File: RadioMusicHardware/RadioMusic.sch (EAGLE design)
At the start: 59 parts, among them IC1 TL074P, IC2 7805L

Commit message: Untested fade circuit + more PCB layout
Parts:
- removed BANK_BUTTON: D6_PUSH_SWITCH, TomW:D6_PUSH_SWITCH
- removed IC1: TL074P, linear:TL074P
- removed R15: 10k, TomW:R-EU_STANDARD_RESISTOR
- added IC3, IC4: TL072P, TomW:TL072P
- added JP1, JP2, JP3, JP4: (no value), SparkFun-Connectors:M08LOCK
- R6: value 8.2k -> 330K
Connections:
- net +3.3V: no longer BANK_BUTTON.P
- net GND: no longer R15.1
- net N$12: now also IC3B.+IN; no longer IC1B.+IN
- net N$2: now also IC4A.+IN; no longer IC1C.+IN
- net N$3: now also IC3A.+IN; no longer IC1A.+IN
- net N$5: now also IC4A.-IN, IC4A.OUT; no longer IC1C.-IN, IC1C.OUT
- net N$6: now also IC4B.+IN; no longer IC1D.+IN
- net N$7: now also IC4B.-IN; no longer IC1D.-IN
- net N$8: now also IC4B.OUT; no longer IC1D.OUT
- net PIN2: no longer BANK_BUTTON.O, R15.2
- net PIN22/A8: now also IC3A.-IN, IC3A.OUT, IC3B.-IN, IC3B.OUT; no longer IC1A.-IN, IC1A.OUT, IC1B.-IN, IC1B.OUT
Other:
- note added: "Front Board requirements: +3.3v for pots & SD Card GND LED1 LED2 LED3 LED4 LEDReset Reset Button Reset CV Time CV Time Pot ChannelCV Channel Pot SD - MISO SD- MOSI SD-CLOCK SD-SS"
- note removed: "NB Outline is for Teensy3 Teensy3.1 has DAC output where Reset was on Teensy3"
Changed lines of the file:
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@@
 <part name="RESET" library="thonkiconn" deviceset="WQP-PJ301M-12_JACK" device=""/>
 <part name="OUT1" library="thonkiconn" deviceset="WQP-PJ301M-12_JACK" device=""/>
-<part name="IC1" library="linear" deviceset="TL074" device="P"/>
 <part name="IC2" library="gm-regulators" deviceset="78*" device="L" technology="05"/>
 <part name="R1" library="TomW" deviceset="R-EU_" device="STANDARD_RESISTOR" value="100k"/>
@@
 <part name="SUPPLY6" library="supply2" deviceset="GND" device=""/>
 <part name="C7" library="TomW" deviceset="C-EU" device="050-025X075" value="100n"/>
-<part name="R6" library="TomW" deviceset="R-EU_" device="STANDARD_RESISTOR" value="8.2k"/>
+<part name="R6" library="TomW" deviceset="R-EU_" device="STANDARD_RESISTOR" value="330K"/>
 <part name="SUPPLY7" library="supply2" deviceset="GND" device=""/>
 <part name="R7" library="TomW" deviceset="R-EU_" device="STANDARD_RESISTOR" value="1k"/>
@@
 <part name="SUPPLY15" library="supply2" deviceset="GND" device=""/>
 <part name="R14" library="TomW" deviceset="R-EU_" device="STANDARD_RESISTOR" value="220R"/>
-<part name="BANK_BUTTON" library="TomW" deviceset="D6_PUSH_SWITCH" device="" value="D6_PUSH_SWITCH"/>
-<part name="R15" library="TomW" deviceset="R-EU_" device="STANDARD_RESISTOR" value="10k"/>
-<part name="SUPPLY18" library="supply2" deviceset="GND" device=""/>
 <part name="RESET_BUTTON" library="TomW" deviceset="D6_PUSH_SWITCH" device="" value="D6_PUSH_SWITCH"/>
 <part name="R16" library="TomW" deviceset="R-EU_" device="STANDARD_RESISTOR" value="10k"/>
@@
 <part name="RESET_LED" library="TomW" deviceset="LED" device="3MM"/>
 <part name="R21" library="TomW" deviceset="R-EU_" device="STANDARD_RESISTOR" value="1k"/>
+<part name="JP1" library="SparkFun-Connectors" deviceset="M08" device="LOCK"/>
+<part name="JP2" library="SparkFun-Connectors" deviceset="M08" device="LOCK"/>
+<part name="JP3" library="SparkFun-Connectors" deviceset="M08" device="LOCK"/>
+<part name="JP4" library="SparkFun-Connectors" deviceset="M08" device="LOCK"/>
+<part name="IC3" library="TomW" deviceset="TL072" device="P"/>
+<part name="IC4" library="TomW" deviceset="TL072" device="P"/>
 </parts>
 <sheets>
@@
 Don't get it the wrong way around!
 Ferrites: 81-BL01RN1A1D2B  or 623-2743001112LF</text>
-<text x="203.2" y="185.42" size="0.762" layer="91">NB Outline is for Teensy3
-Teensy3.1 has DAC output
-where Reset was on Teensy3</text>
 <text x="243.84" y="137.16" size="1.27" layer="91"> SD Card Connections:
  SCLK 14
@@
  MOSI 7
  SS   10 </text>
+<text x="248.92" y="182.88" size="0.762" layer="91">Front Board requirements:
++3.3v for pots &amp; SD Card
+GND
+LED1
+LED2
+LED3
+LED4
+LEDReset
+Reset Button
+Reset CV
+Time CV
+Time Pot
+ChannelCV
+Channel Pot
+SD - MISO
+SD- MOSI
+SD-CLOCK
+SD-SS
+</text>
 </plain>
 <instances>
@@
 <instance part="RESET" gate="G$1" x="119.38" y="134.62" rot="MR0"/>
 <instance part="OUT1" gate="G$1" x="269.24" y="66.04"/>
-<instance part="IC1" gate="A" x="66.04" y="157.48"/>
-<instance part="IC1" gate="C" x="182.88" y="71.12"/>
-<instance part="IC1" gate="D" x="231.14" y="68.58"/>
+<instance part="IC3" gate="A" x="66.04" y="157.48"/>
+<instance part="IC4" gate="A" x="182.88" y="71.12"/>
+<instance part="IC4" gate="B" x="231.14" y="68.58"/>
 <instance part="IC2" gate="A1" x="91.44" y="38.1"/>
 <instance part="R1" gate="G$1" x="45.72" y="160.02"/>
@@
 <instance part="TIME" gate="G$1" x="20.32" y="66.04"/>
 <instance part="TIME_CV" gate="G$1" x="20.32" y="96.52" rot="MR0"/>
-<instance part="IC1" gate="B" x="66.04" y="96.52"/>
+<instance part="IC3" gate="B" x="66.04" y="96.52"/>
 <instance part="R10" gate="G$1" x="45.72" y="99.06"/>
 <instance part="SUPPLY9" gate="GND" x="25.4" y="88.9"/>
@@
 <instance part="SUPPLY15" gate="GND" x="157.48" y="116.84"/>
 <instance part="R14" gate="G$1" x="134.62" y="137.16"/>
-<instance part="BANK_BUTTON" gate="G$1" x="127" y="198.12"/>
-<instance part="R15" gate="G$1" x="134.62" y="190.5" rot="R90"/>
-<instance part="SUPPLY18" gate="GND" x="134.62" y="180.34"/>
 <instance part="RESET_BUTTON" gate="G$1" x="165.1" y="198.12"/>
 <instance part="R16" gate="G$1" x="172.72" y="190.5" rot="R90"/>
@@
 <instance part="RESET_LED" gate="G$1" x="185.42" y="144.78" rot="R270"/>
 <instance part="R21" gate="G$1" x="170.18" y="144.78"/>
+<instance part="JP1" gate="G$1" x="304.8" y="190.5"/>
+<instance part="JP2" gate="G$1" x="317.5" y="198.12"/>
+<instance part="JP3" gate="G$1" x="307.34" y="167.64"/>
+<instance part="JP4" gate="G$1" x="320.04" y="170.18"/>
 </instances>
 <busses>
@@
 <wire x1="157.48" y1="121.92" x2="157.48" y2="119.38" width="0.1524" layer="91"/>
 <pinref part="SUPPLY15" gate="GND" pin="GND"/>
-</segment>
-<segment>
-<pinref part="R15" gate="G$1" pin="1"/>
-<wire x1="134.62" y1="185.42" x2="134.62" y2="182.88" width="0.1524" layer="91"/>
-<pinref part="SUPPLY18" gate="GND" pin="GND"/>
 </segment>
 <segment>
@@
 </segment>
 <segment>
-<pinref part="BANK_BUTTON" gate="G$1" pin="P"/>
-<wire x1="119.38" y1="198.12" x2="121.92" y2="198.12" width="0.1524" layer="91"/>
-<label x="119.38" y="198.12" size="1.27" layer="95" rot="R180" xref="yes"/>
-</segment>
-<segment>
 <pinref part="RESET_BUTTON" gate="G$1" pin="P"/>
 <wire x1="157.48" y1="198.12" x2="160.02" y2="198.12" width="0.1524" layer="91"/>
@@
 <segment>
 <pinref part="R1" gate="G$1" pin="2"/>
-<pinref part="IC1" gate="A" pin="+IN"/>
+<pinref part="IC3" gate="A" pin="+IN"/>
 <wire x1="58.42" y1="160.02" x2="50.8" y2="160.02" width="0.1524" layer="91"/>
 </segment>
@@
 <net name="PIN22/A8" class="0">
 <segment>
-<pinref part="IC1" gate="A" pin="-IN"/>
+<pinref part="IC3" gate="A" pin="-IN"/>
 <wire x1="58.42" y1="154.94" x2="53.34" y2="154.94" width="0.1524" layer="91"/>
 <wire x1="53.34" y1="154.94" x2="53.34" y2="147.32" width="0.1524" layer="91"/>
 <wire x1="53.34" y1="147.32" x2="78.74" y2="147.32" width="0.1524" layer="91"/>
 <wire x1="78.74" y1="147.32" x2="78.74" y2="157.48" width="0.1524" layer="91"/>
-<pinref part="IC1" gate="A" pin="OUT"/>
+<pinref part="IC3" gate="A" pin="OUT"/>
 <wire x1="78.74" y1="157.48" x2="73.66" y2="157.48" width="0.1524" layer="91"/>
 <pinref part="R9" gate="G$1" pin="1"/>
@@
 </segment>
 <segment>
-<pinref part="IC1" gate="B" pin="-IN"/>
+<pinref part="IC3" gate="B" pin="-IN"/>
 <wire x1="58.42" y1="93.98" x2="53.34" y2="93.98" width="0.1524" layer="91"/>
 <wire x1="53.34" y1="93.98" x2="53.34" y2="86.36" width="0.1524" layer="91"/>
 <wire x1="53.34" y1="86.36" x2="78.74" y2="86.36" width="0.1524" layer="91"/>
 <wire x1="78.74" y1="86.36" x2="78.74" y2="96.52" width="0.1524" layer="91"/>
-<pinref part="IC1" gate="B" pin="OUT"/>
+<pinref part="IC3" gate="B" pin="OUT"/>
 <wire x1="78.74" y1="96.52" x2="73.66" y2="96.52" width="0.1524" layer="91"/>
 <pinref part="R12" gate="G$1" pin="1"/>
@@
 <net name="N$2" class="0">
 <segment>
-<pinref part="IC1" gate="C" pin="+IN"/>
+<pinref part="IC4" gate="A" pin="+IN"/>
 <pinref part="R3" gate="G$1" pin="2"/>
 <wire x1="167.64" y1="73.66" x2="170.18" y2="73.66" width="0.1524" layer="91"/>
@@
 <wire x1="177.8" y1="83.82" x2="195.58" y2="83.82" width="0.1524" layer="91"/>
 <wire x1="195.58" y1="83.82" x2="195.58" y2="71.12" width="0.1524" layer="91"/>
-<pinref part="IC1" gate="C" pin="OUT"/>
+<pinref part="IC4" gate="A" pin="OUT"/>
 <wire x1="195.58" y1="71.12" x2="190.5" y2="71.12" width="0.1524" layer="91"/>
-<pinref part="IC1" gate="C" pin="-IN"/>
+<pinref part="IC4" gate="A" pin="-IN"/>
 <wire x1="175.26" y1="68.58" x2="172.72" y2="68.58" width="0.1524" layer="91"/>
 <wire x1="172.72" y1="68.58" x2="172.72" y2="63.5" width="0.1524" layer="91"/>
@@
 <segment>
 <pinref part="C7" gate="G$1" pin="1"/>
-<pinref part="IC1" gate="D" pin="+IN"/>
+<pinref part="IC4" gate="B" pin="+IN"/>
 <wire x1="208.28" y1="71.12" x2="213.36" y2="71.12" width="0.1524" layer="91"/>
 <wire x1="213.36" y1="71.12" x2="223.52" y2="71.12" width="0.1524" layer="91"/>
@@
 <net name="N$7" class="0">
 <segment>
-<pinref part="IC1" gate="D" pin="-IN"/>
+<pinref part="IC4" gate="B" pin="-IN"/>
 <pinref part="R7" gate="G$1" pin="2"/>
 <wire x1="223.52" y1="66.04" x2="220.98" y2="66.04" width="0.1524" layer="91"/>
@@
 <net name="N$8" class="0">
 <segment>
-<pinref part="IC1" gate="D" pin="OUT"/>
+<pinref part="IC4" gate="B" pin="OUT"/>
 <pinref part="R4" gate="G$1" pin="1"/>
 <wire x1="238.76" y1="68.58" x2="243.84" y2="68.58" width="0.1524" layer="91"/>
@@
 <segment>
 <pinref part="R10" gate="G$1" pin="2"/>
-<pinref part="IC1" gate="B" pin="+IN"/>
+<pinref part="IC3" gate="B" pin="+IN"/>
 <wire x1="58.42" y1="99.06" x2="50.8" y2="99.06" width="0.1524" layer="91"/>
 </segment>
@@
 <net name="PIN2" class="0">
 <segment>
-<pinref part="BANK_BUTTON" gate="G$1" pin="O"/>
-<wire x1="132.08" y1="198.12" x2="134.62" y2="198.12" width="0.1524" layer="91"/>
-<wire x1="134.62" y1="198.12" x2="139.7" y2="198.12" width="0.1524" layer="91"/>
-<pinref part="R15" gate="G$1" pin="2"/>
-<wire x1="134.62" y1="195.58" x2="134.62" y2="198.12" width="0.1524" layer="91"/>
-<junction x="134.62" y="198.12"/>
-<label x="139.7" y="198.12" size="1.27" layer="95" xref="yes"/>
-</segment>
-<segment>
 <pinref part="U$1" gate="G$1" pin="2"/>

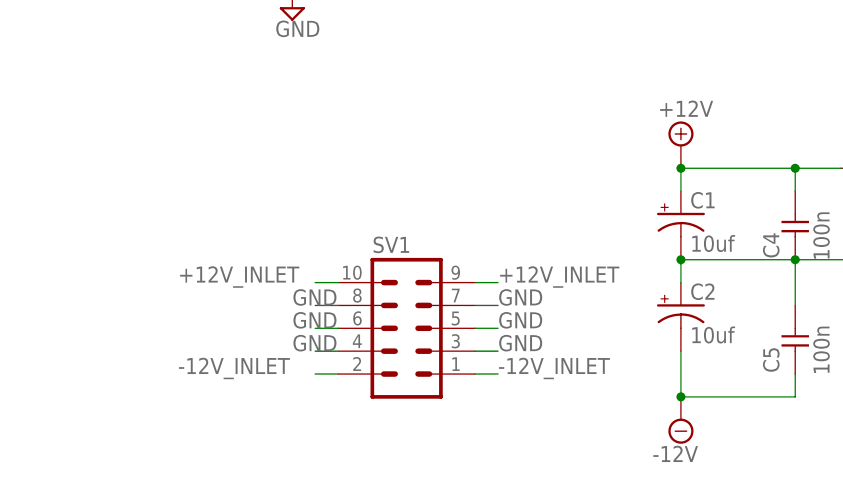
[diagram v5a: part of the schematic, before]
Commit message: Power to op amps!
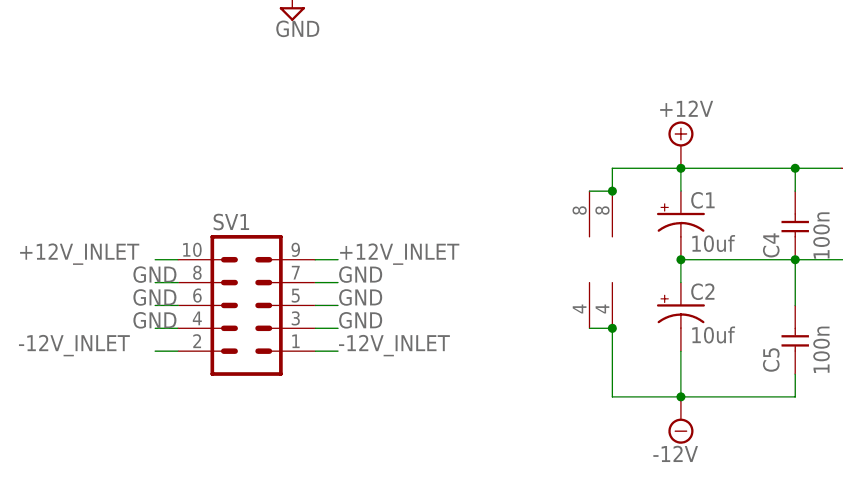
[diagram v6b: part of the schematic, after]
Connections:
- net +12V: now also IC3P.V+, IC4P.V+
- net -12V: now also IC3P.V-, IC4P.V-
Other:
- moved on the sheet: SV1
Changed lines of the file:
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@@
 </variantdefs>
 <classes>
-<class number="0" name="default" width="0.6096" drill="0">
+<class number="0" name="default" width="0.2032" drill="0">
 </class>
-<class number="1" name="power" width="0.6096" drill="0">
+<class number="1" name="power" width="0.2032" drill="0">
 </class>
-<class number="2" name="ground" width="0.6096" drill="0">
+<class number="2" name="ground" width="0.2032" drill="0">
 </class>
 </classes>
@@
 <instances>
 <instance part="CHANNEL" gate="G$1" x="20.32" y="127"/>
-<instance part="SV1" gate="G$1" x="33.02" y="20.32"/>
+<instance part="SV1" gate="G$1" x="15.24" y="22.86"/>
 <instance part="SUPPLY16" gate="G$1" x="63.5" y="10.16"/>
 <instance part="SUPPLY17" gate="+12V" x="63.5" y="40.64"/>
@@
 <instance part="JP3" gate="G$1" x="307.34" y="167.64"/>
 <instance part="JP4" gate="G$1" x="320.04" y="170.18"/>
+<instance part="IC3" gate="P" x="53.34" y="27.94"/>
+<instance part="IC4" gate="P" x="55.88" y="27.94"/>
 </instances>
 <busses>
@@
 <segment>
 <pinref part="SV1" gate="G$1" pin="7"/>
-<wire x1="43.18" y1="22.86" x2="40.64" y2="22.86" width="0.1524" layer="91"/>
-<label x="43.18" y="22.86" size="1.778" layer="95"/>
+<wire x1="25.4" y1="25.4" x2="22.86" y2="25.4" width="0.1524" layer="91"/>
+<label x="25.4" y="25.4" size="1.778" layer="95"/>
 </segment>
 <segment>
 <pinref part="SV1" gate="G$1" pin="5"/>
-<wire x1="43.18" y1="20.32" x2="40.64" y2="20.32" width="0.1524" layer="91"/>
-<label x="43.18" y="20.32" size="1.778" layer="95"/>
+<wire x1="25.4" y1="22.86" x2="22.86" y2="22.86" width="0.1524" layer="91"/>
+<label x="25.4" y="22.86" size="1.778" layer="95"/>
 </segment>
 <segment>
 <pinref part="SV1" gate="G$1" pin="3"/>
-<wire x1="43.18" y1="17.78" x2="40.64" y2="17.78" width="0.1524" layer="91"/>
-<label x="43.18" y="17.78" size="1.778" layer="95"/>
+<wire x1="25.4" y1="20.32" x2="22.86" y2="20.32" width="0.1524" layer="91"/>
+<label x="25.4" y="20.32" size="1.778" layer="95"/>
 </segment>
 <segment>
 <pinref part="SV1" gate="G$1" pin="8"/>
-<wire x1="22.86" y1="22.86" x2="25.4" y2="22.86" width="0.1524" layer="91"/>
-<label x="20.32" y="22.86" size="1.778" layer="95"/>
+<wire x1="5.08" y1="25.4" x2="7.62" y2="25.4" width="0.1524" layer="91"/>
+<label x="2.54" y="25.4" size="1.778" layer="95"/>
 </segment>
 <segment>
 <pinref part="SV1" gate="G$1" pin="6"/>
-<wire x1="22.86" y1="20.32" x2="25.4" y2="20.32" width="0.1524" layer="91"/>
-<label x="20.32" y="20.32" size="1.778" layer="95"/>
+<wire x1="5.08" y1="22.86" x2="7.62" y2="22.86" width="0.1524" layer="91"/>
+<label x="2.54" y="22.86" size="1.778" layer="95"/>
 </segment>
 <segment>
 <pinref part="SV1" gate="G$1" pin="4"/>
-<wire x1="22.86" y1="17.78" x2="25.4" y2="17.78" width="0.1524" layer="91"/>
-<label x="20.32" y="17.78" size="1.778" layer="95"/>
+<wire x1="5.08" y1="20.32" x2="7.62" y2="20.32" width="0.1524" layer="91"/>
+<label x="2.54" y="20.32" size="1.778" layer="95"/>
 </segment>
 <segment>
@@
 <wire x1="81.28" y1="38.1" x2="76.2" y2="38.1" width="0.1524" layer="91"/>
 <junction x="76.2" y="38.1"/>
+<pinref part="IC3" gate="P" pin="V+"/>
+<pinref part="IC4" gate="P" pin="V+"/>
+<wire x1="53.34" y1="35.56" x2="55.88" y2="35.56" width="0.1524" layer="91"/>
+<wire x1="55.88" y1="35.56" x2="55.88" y2="38.1" width="0.1524" layer="91"/>
+<junction x="55.88" y="35.56"/>
+<wire x1="55.88" y1="38.1" x2="63.5" y2="38.1" width="0.1524" layer="91"/>
 </segment>
 <segment>
@@
 <wire x1="76.2" y1="12.7" x2="63.5" y2="12.7" width="0.1524" layer="91"/>
 <junction x="63.5" y="12.7"/>
+<pinref part="IC3" gate="P" pin="V-"/>
+<pinref part="IC4" gate="P" pin="V-"/>
+<wire x1="53.34" y1="20.32" x2="55.88" y2="20.32" width="0.1524" layer="91"/>
+<wire x1="63.5" y1="12.7" x2="55.88" y2="12.7" width="0.1524" layer="91"/>
+<wire x1="55.88" y1="12.7" x2="55.88" y2="20.32" width="0.1524" layer="91"/>
+<junction x="55.88" y="20.32"/>
 </segment>
 <segment>
@@
 <segment>
 <pinref part="SV1" gate="G$1" pin="10"/>
-<wire x1="22.86" y1="25.4" x2="25.4" y2="25.4" width="0.1524" layer="91"/>
-<label x="7.62" y="25.4" size="1.778" layer="95"/>
+<wire x1="5.08" y1="27.94" x2="7.62" y2="27.94" width="0.1524" layer="91"/>
+<label x="-10.16" y="27.94" size="1.778" layer="95"/>
 </segment>
 <segment>
 <pinref part="SV1" gate="G$1" pin="9"/>
-<wire x1="43.18" y1="25.4" x2="40.64" y2="25.4" width="0.1524" layer="91"/>
-<label x="43.18" y="25.4" size="1.778" layer="95"/>
+<wire x1="25.4" y1="27.94" x2="22.86" y2="27.94" width="0.1524" layer="91"/>
+<label x="25.4" y="27.94" size="1.778" layer="95"/>
 </segment>
 <segment>
@@
 <segment>
 <pinref part="SV1" gate="G$1" pin="1"/>
-<wire x1="43.18" y1="15.24" x2="40.64" y2="15.24" width="0.1524" layer="91"/>
-<label x="43.18" y="15.24" size="1.778" layer="95"/>
+<wire x1="25.4" y1="17.78" x2="22.86" y2="17.78" width="0.1524" layer="91"/>
+<label x="25.4" y="17.78" size="1.778" layer="95"/>
 </segment>
 <segment>
 <pinref part="SV1" gate="G$1" pin="2"/>
-<wire x1="22.86" y1="15.24" x2="25.4" y2="15.24" width="0.1524" layer="91"/>
-<label x="7.62" y="15.24" size="1.778" layer="95"/>
-</segment>
-<segment>
+<wire x1="5.08" y1="17.78" x2="7.62" y2="17.78" width="0.1524" layer="91"/>
+<label x="-10.16" y="17.78" size="1.778" layer="95"/>
+</segment>
+<segment>
